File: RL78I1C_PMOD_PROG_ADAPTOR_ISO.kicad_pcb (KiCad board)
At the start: 2 copper layers, 50 x 30 mm, 26 parts, among them J1 E2 Lite 14P, J2 RL78/I1C 5P, Q1 MMBT3906-7-F, U1 RV1S9060A, U2 RV1S9060A, U3 RV1S9060A, U4 RV1S9060A, U5 SN74LVC1G17, U6 SN74LVC1G17

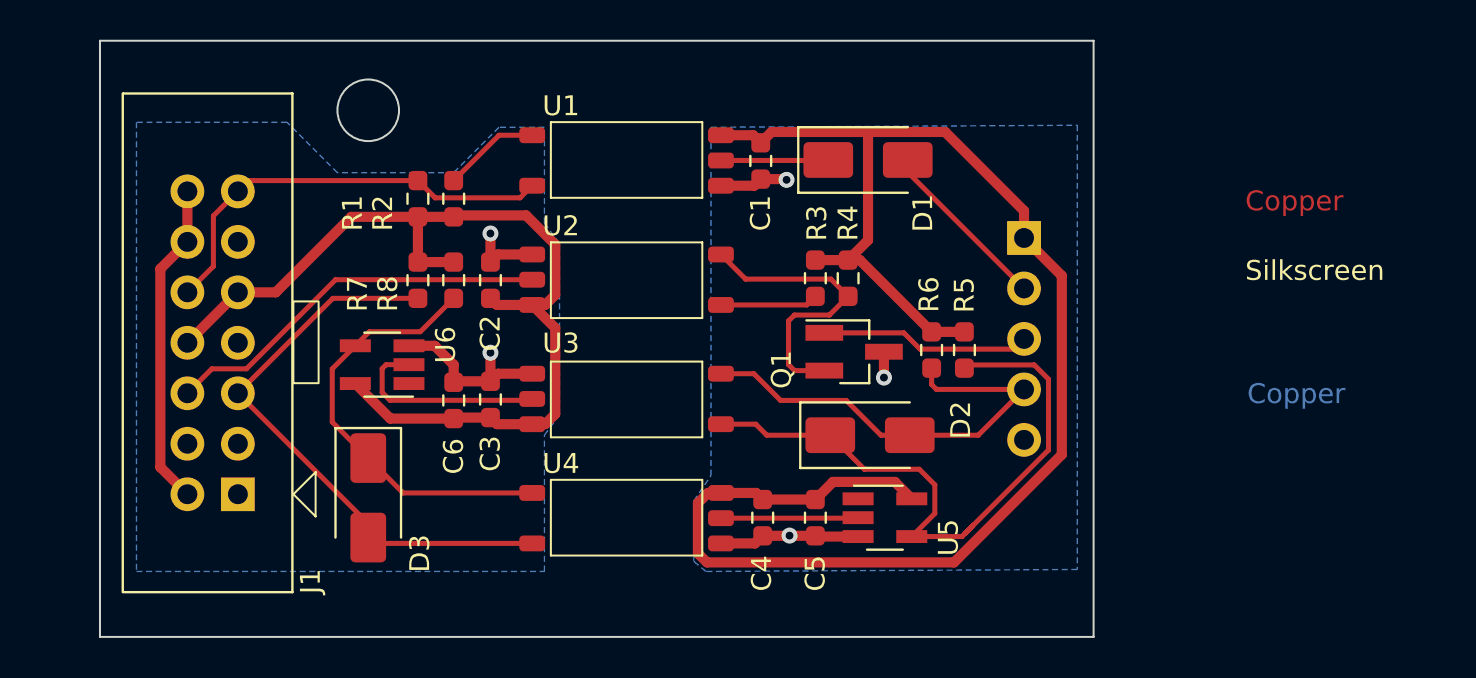
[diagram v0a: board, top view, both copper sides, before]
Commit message: Fixed PCB using FET's instead of buffers.
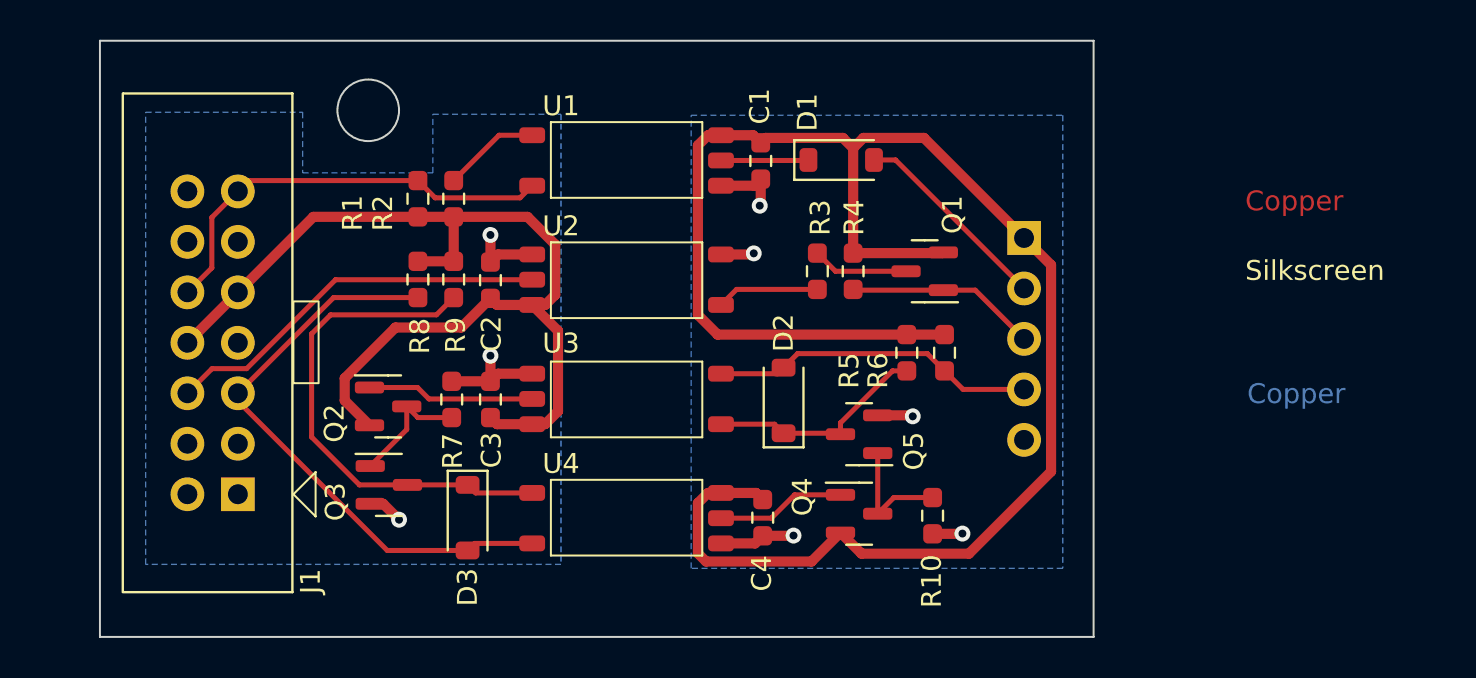
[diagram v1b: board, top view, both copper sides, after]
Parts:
- removed C5, C6: 100n, 0_Common:R_0603_1608Metric_Pad0.98x0.95mm_HandSolder
- removed U5, U6: SN74LVC1G17, 0_Common:SOT-23-5_HandSoldering
- added Q2: BSS84, 0_Common:SOT-23, F.Cu at (110.5, 115.9)
- added Q3: BSS123, 0_Common:SOT-23, F.Cu at (110.5, 119.8)
- added Q4: BSS84, 0_Common:SOT-23, F.Cu at (134.2, 121.3)
- added Q5: BSS123, 0_Common:SOT-23, F.Cu at (134.2, 117.3)
- added R10: 220R, 0_Common:R_0603_1608Metric_Pad0.98x0.95mm_HandSolder, F.Cu at (137.9, 121.4)
- added R9: 270R, 0_Common:R_0603_1608Metric_Pad0.98x0.95mm_HandSolder, F.Cu at (113.8, 109.5)
- D1, D2, D3: value CDBA340L-G -> BAT43W-TP; footprint 0_Common:D_SMA -> 0_Common:D_SOD-123
- Q1: value MMBT3906-7-F -> BSS84; footprint 0_Common:SOT-23_Handsoldering -> 0_Common:SOT-23
- R7: value 4k7 -> 220R
- R8: value 270R -> 4k7
- moved R7 6.24 mm to (113.7, 115.5), turned to 90 degrees
- moved Q1 5.39 mm to (137.5, 109.1), turned to 180 degrees
- moved D3 5.10 mm to (114.5, 121.5)
- moved D2 4.69 mm to (130.4, 115.6), turned to 90 degrees
- moved R5 2.90 mm to (136.6, 113.2)
- moved R8 1.80 mm to (112.0, 109.5)
- moved D1 1.35 mm to (133.3, 103.5)
- moved R6 0.66 mm to (138.5, 113.2)
- moved R4 0.43 mm to (133.9, 109.1)
- moved R3 0.36 mm to (132.1, 109.1)
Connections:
- Q1 pad 2: Net-(Q1-E) -> VCOM
- Q1 pad 3: GNDD -> Net-(Q1-D)
- R3 pad 1: VCOM -> Net-(Q1-D)
- R4 pad 2: Net-(Q1-E) -> /~{RESET_OUT_MCU}
- R7 pad 1: VCC -> Net-(Q2-D)
- R7 pad 2: /TOOL0 -> GND
- R8 pad 2: Net-(D3-K) -> /TOOL0
- U2 pad 2: Net-(Q1-E) -> GNDD
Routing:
- net Net-(D2-K): track 32.5 -> 11.2 mm
- net GND: track 29.3 -> 10.9 mm, vias 2 -> 3
- net Net-(Q1-E): track 14.9 -> 0.00 mm
- net VCOM: track 81.3 -> 89.7 mm
- net /TOOL0_MCU: track 23.1 -> 16.4 mm
- net Net-(Q2-D): track 0.00 -> 6.26 mm
- net Net-(Q4-D): track 0.00 -> 6.15 mm
- net Net-(Q1-D): track 0.00 -> 4.84 mm
- net VCC: track 49.1 -> 53.5 mm
- net Net-(D3-K): track 21.8 -> 25.4 mm
- net Net-(Q2-G): track 10.4 -> 8.43 mm
- net /~{RESET_IN_MCU}: track 8.89 -> 10.2 mm
- net Net-(D1-K): track 5.41 -> 4.41 mm
- net /~{RESET_OUT_MCU}: track 10.6 -> 9.63 mm
- net GNDD: track 11.8 -> 12.3 mm, vias 3 -> 5
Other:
- board text added: "Title: RL78I1C_PMOD_PROG_ADAPTOR_ISO Version: 2.00 Date: 02/08/2024"
- board text removed: "Title: RL78I1C_PMOD_PROG_ADAPTOR_ISO Version: 1.00 Date: 16/02/2024"

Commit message: Finished version 1 - ready for assembly.
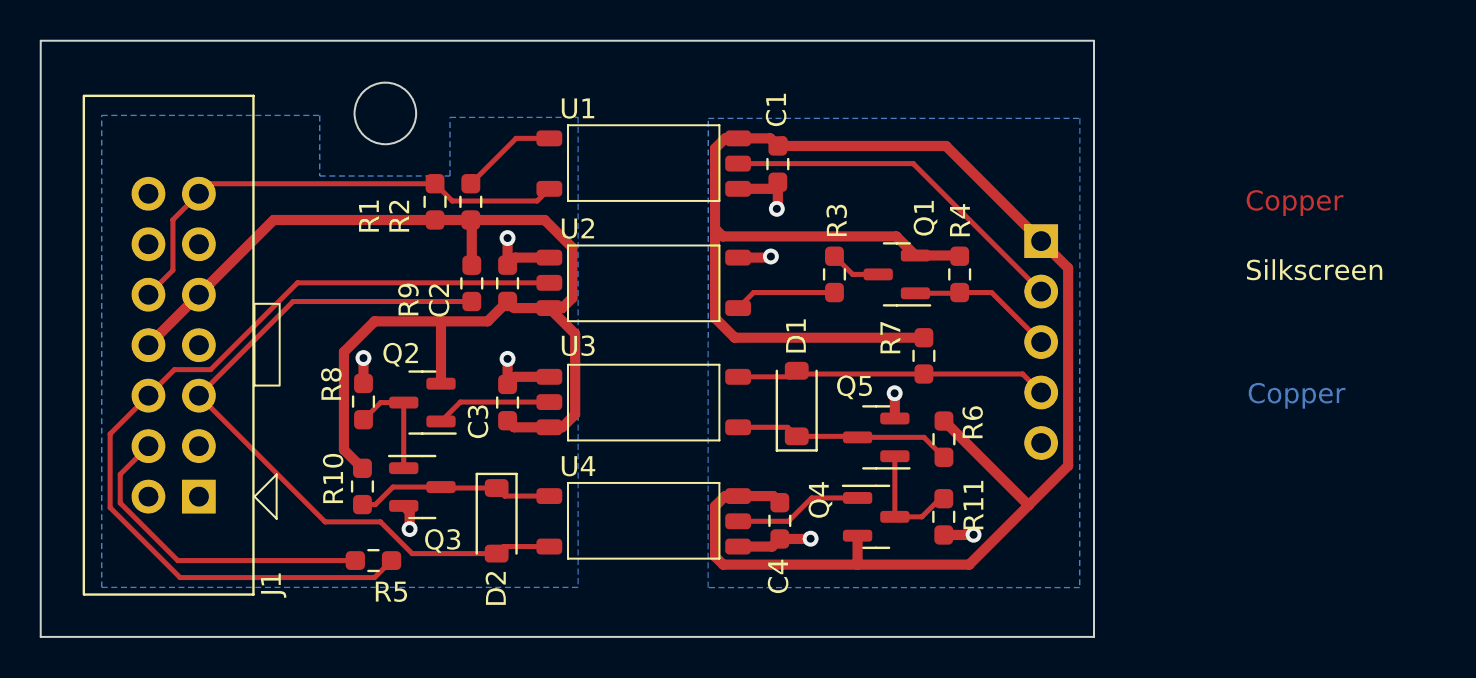
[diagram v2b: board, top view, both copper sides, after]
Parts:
- removed D3: BAT43W-TP, 0_Common:D_SOD-123
- added R11: 220R, 0_Common:R_0603_1608Metric_Pad0.98x0.95mm_HandSolder, F.Cu at (138.5, 121.5)
- R10: value 220R -> 270R
- R5: value 270R -> 1k
- R6: value 4k7 -> 270R
- R7: value 220R -> 4k7
- R8: value 4k7 -> 220R
- R9: value 270R -> 4k7
- moved R5 28.8 mm to (109.8, 123.7), turned to 0 degrees
- moved R10 28.7 mm to (109.2, 119.9)
- moved R7 23.9 mm to (137.5, 113.4), turned to -90 degrees
- moved D2 15.7 mm to (116.0, 121.7), turned to -90 degrees
- moved D1 12.5 mm to (131.1, 115.8), turned to 90 degrees
- moved R8 6.73 mm to (109.3, 115.7), turned to 90 degrees
- moved R4 5.36 mm to (139.3, 109.3)
- moved R6 4.35 mm to (138.5, 117.5)
- moved J1 1.96 mm to (101.0, 120.4)
- moved Q2 1.73 mm to (112.2, 115.7), turned to 180 degrees
- moved Q3 1.69 mm to (112.2, 120.0)
- moved Q1 1.41 mm to (136.1, 109.3)
- moved R9 0.93 mm to (114.7, 109.7)
- moved C1 0.88 mm to (130.1, 103.7)
- moved C4 0.88 mm to (130.2, 121.7)
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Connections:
- D1 pad 2: /~{RESET_IN_MCU} -> /TOOL0_MCU
- D2 pad 2: /TOOL0_MCU -> /TOOL0
- J1 pad 4: unconnected-(J1-Pin_4-Pad4) -> Net-(J1-Pin_4)
- Q3 pad 3: Net-(D3-K) -> Net-(D2-K)
- Q5 pad 3: Net-(D2-K) -> Net-(D1-K)
- R10 pad 1: Net-(Q4-D) -> VCC
- R10 pad 2: GNDD -> Net-(D2-K)
- R5 pad 1: VCOM -> Net-(J1-Pin_4)
- R5 pad 2: Net-(D2-K) -> /~{RESET_IN}
- R6 pad 2: /TOOL0_MCU -> Net-(D1-K)
- R7 pad 1: Net-(Q2-D) -> VCOM
- R7 pad 2: GND -> /TOOL0_MCU
- R8 pad 1: VCC -> Net-(Q2-D)
- R8 pad 2: /TOOL0 -> GND
- R9 pad 2: Net-(D3-K) -> /TOOL0
- U1 pad 4: Net-(D1-K) -> /~{RESET_IN_MCU}
- U3 pad 1: Net-(D2-K) -> Net-(D1-K)
- U4 pad 1: Net-(D3-K) -> Net-(D2-K)
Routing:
- net Net-(D3-K): track 25.4 -> 0.00 mm
- net /~{RESET_IN}: track 19.7 -> 45.0 mm
- net Net-(J1-Pin_4): track 0.00 -> 16.5 mm
- net VCC: track 53.5 -> 61.3 mm
- net /~{RESET_IN_MCU}: track 10.2 -> 17.9 mm
- net /TOOL0: track 29.5 -> 36.8 mm
- net VCOM: track 89.7 -> 96.9 mm
- net Net-(D1-K): track 4.41 -> 11.0 mm
- net /~{RESET_OUT}: track 21.8 -> 24.6 mm
- net Net-(Q2-G): track 8.43 -> 5.85 mm
- net Net-(Q1-D): track 4.84 -> 2.58 mm
- net /~{RESET_OUT_MCU}: track 9.63 -> 7.37 mm
- net Net-(D2-K): track 11.2 -> 9.96 mm
- net GND: track 10.9 -> 9.80 mm, vias 3 -> 4
- net /TOOL0_MCU: track 16.4 -> 15.8 mm
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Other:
- board size 50 x 30 mm -> 53 x 30 mm
- board text added: "RL78/I1C PMOD Programming Adaptor V1.00 5kv 15Mbps Isolation"
- board text added: "Title: RL78I1C_PMOD_PROG_ADAPTOR_ISO Version: 1.00 Date: 22/10/2024"
- board text removed: "RL78/I1C PMOD Programming Adaptor V2.00 5kv 15Mbps Isolation"
- board text removed: "Title: RL78I1C_PMOD_PROG_ADAPTOR_ISO Version: 2.00 Date: 02/08/2024"
